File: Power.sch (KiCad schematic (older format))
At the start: 0 parts

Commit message: Blocked out the LED Driver and Power sheets
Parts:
- added C? (x2): C, ~, symbol C
- added F? (x4): FUSE, ~, symbol FUSE
- added L? (x2): INDUCTOR, ~, symbol INDUCTOR
- added P?: CONN_12X2, symbol CONN_12X2
- added R?: R, ~, symbol R
- added SW?: SWITCH_INV, ~, symbol SWITCH_INV
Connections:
- net labels added: +12P, +12V, +3.3V, +5V, -12P, -12V, GND
- wire segments 0 -> 43
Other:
- note added: "12V Power Filtering"
- note added: "24Pin Molex from ATX Power Supply"
- note added: "Main Power Switch"
- note added: "Power from ATX Power Supply\nFuses are PTC Resettable"

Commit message: Completed Arduino Block Diagram and Fan Redesign
The commits as of this are now up to date with the videos released for
Contextual Electronics, Week 3.
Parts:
- removed F? (x4): FUSE, ~, symbol FUSE
- added TH? (x4): THERMISTOR, ~, symbol THERMISTOR
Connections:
- net labels added: +12C
- wire segments 43 -> 44
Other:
- note added: "+12v for current sense\nin fan module"
- note added: "PTC Resettable\nFuses"
- note added: "Unfiltered Power Rails"
- note removed: "Power from ATX Power Supply\nFuses are PTC Resettable"
- moved on the sheet: C?, L?

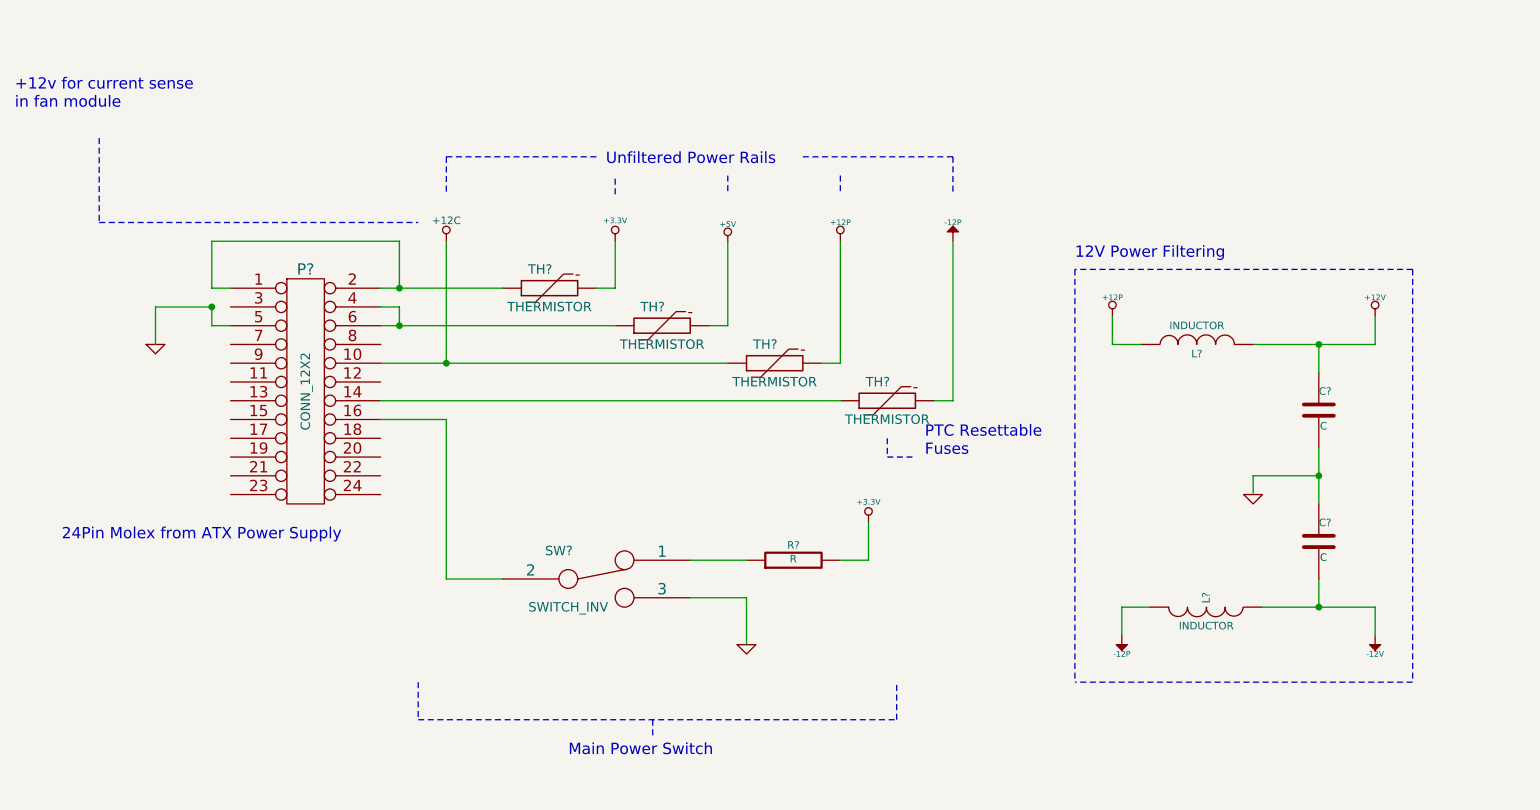
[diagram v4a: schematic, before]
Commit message: Initial layout of relay and thermocouple
All block diagrams completed through Week 3.  Component selection
spreadsheets created: Bench Buddy Session 1CE.xlsx = official part
selection and bom.xlsx is the version I came up with.

Part association and initial layout of the Relay and Thermocouple
sections completed.
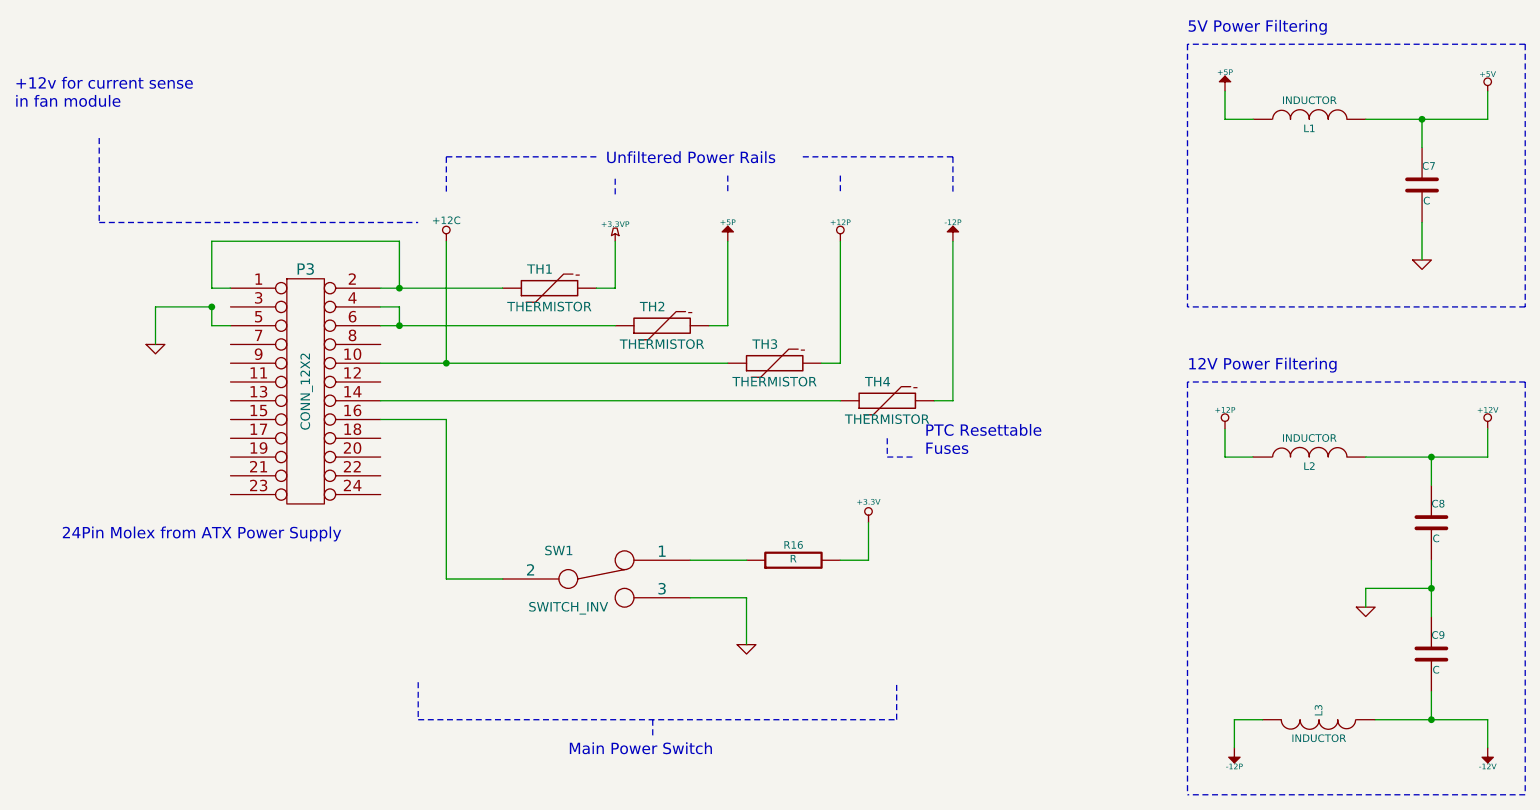
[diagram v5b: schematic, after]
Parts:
- removed C? (x2): C, ~, symbol C
- added C7, C8, C9: C, ~, symbol C
- added L1: INDUCTOR, ~, symbol INDUCTOR
- gave numbers to parts that had none: 9
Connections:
- net +12V: now also C8.1
- net +3.3V: no longer TH1.2
- net +5V: now also C7.1, L1.2; no longer TH2.2
- net -12V: now also C9.2
- net GND: now also C7.2, C8.2, C9.1
- new net +3.3VP: TH1.2
- new net +5P: L1.1, TH2.2
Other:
- note added: "5V Power Filtering"
- moved on the sheet: L2, L3

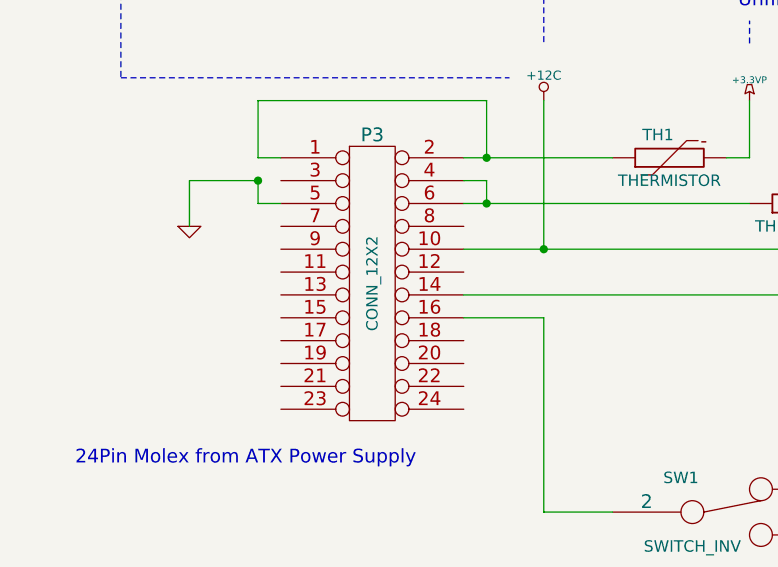
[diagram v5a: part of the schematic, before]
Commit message: Initial layout of Arduino and Fan-Current
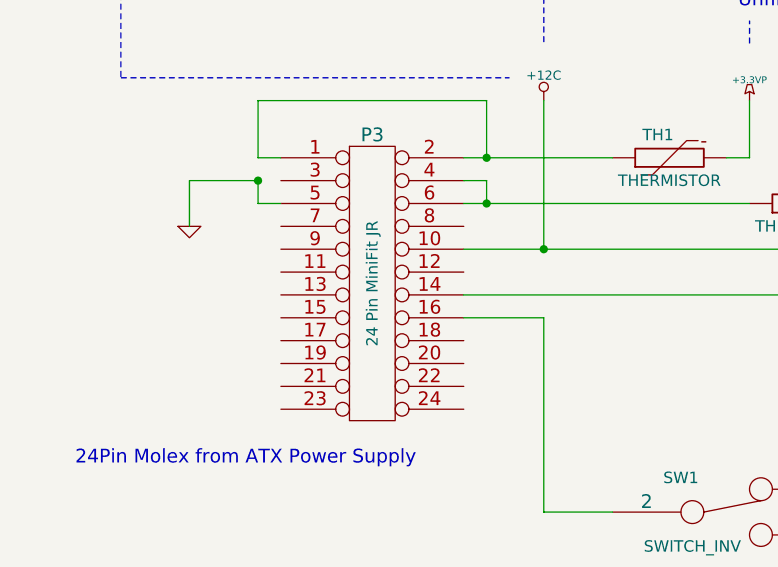
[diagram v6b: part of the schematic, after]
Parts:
- P3: value CONN_12X2 -> 24 Pin MiniFit JR; Distrib Part Num 1 (none) -> 538-39-30-1240; MFG Name (none) -> Molex; MFG Part Num (none) -> 39-30-1240
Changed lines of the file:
@@
 Sheet 4 9
 Title ""
-Date "21 feb 2014"
+Date "22 feb 2014"
 Rev ""
 Comp ""
@@
 P 3500 3750
 F 0 "P3" H 3500 4400 60  0000 C CNN
-F 1 "CONN_12X2" V 3500 3750 50  0000 C CNN
+F 1 "24 Pin MiniFit JR" V 3500 3750 50  0000 C CNN
 F 2 "" H 3500 3750 60  0000 C CNN
 F 3 "" H 3500 3750 60  0000 C CNN
+F 4 "Molex" H 3500 3750 60  0001 C CNN "MFG Name"
+F 5 "39-30-1240" H 3500 3750 60  0001 C CNN "MFG Part Num"
+F 6 "538-39-30-1240" H 3500 3750 60  0001 C CNN "Distrib Part Num 1"
 	1    3500 3750
 	1    0    0    -1

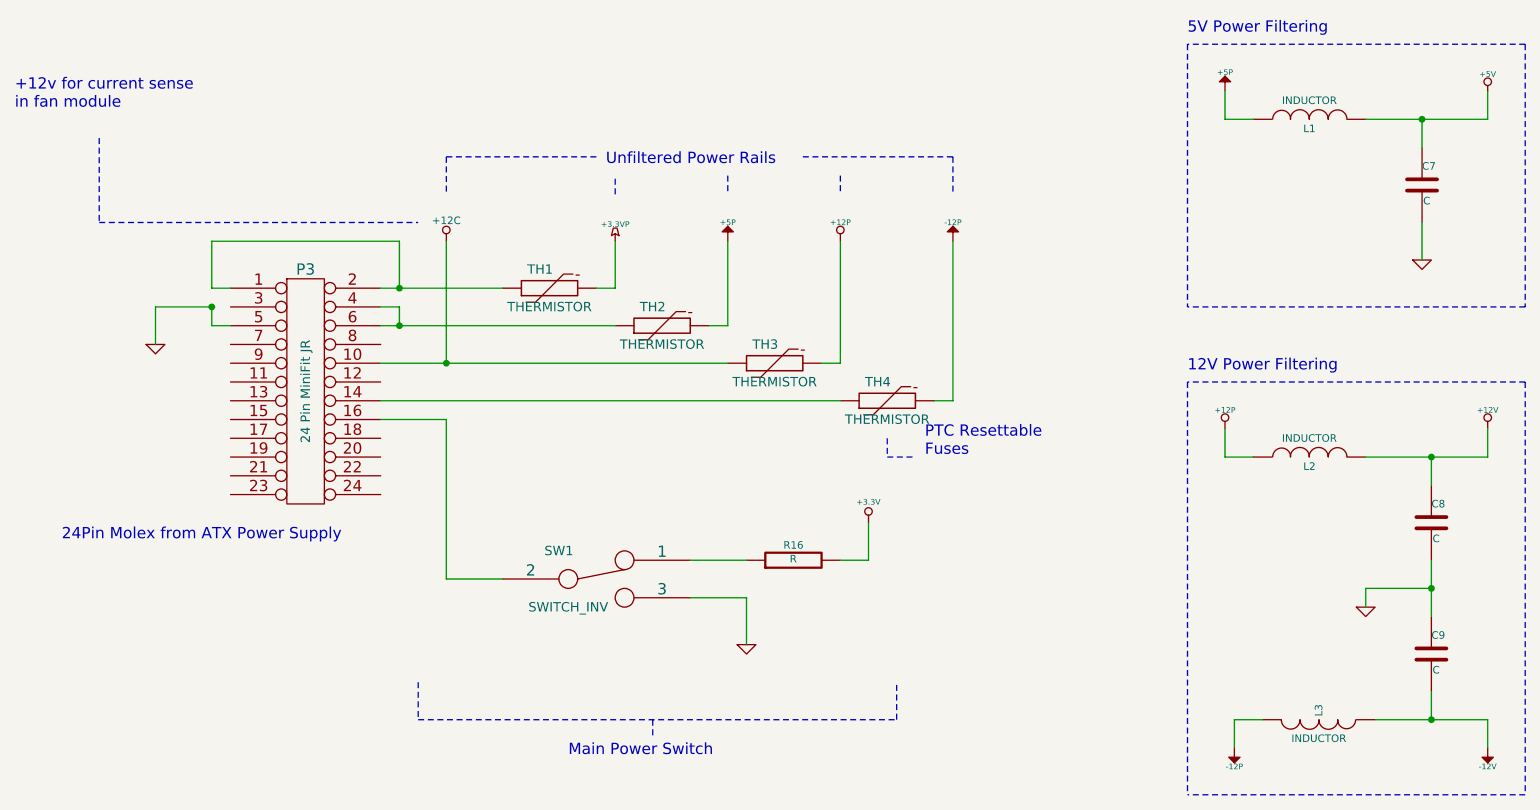
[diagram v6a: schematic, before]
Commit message: Reorganization of power conditioning module
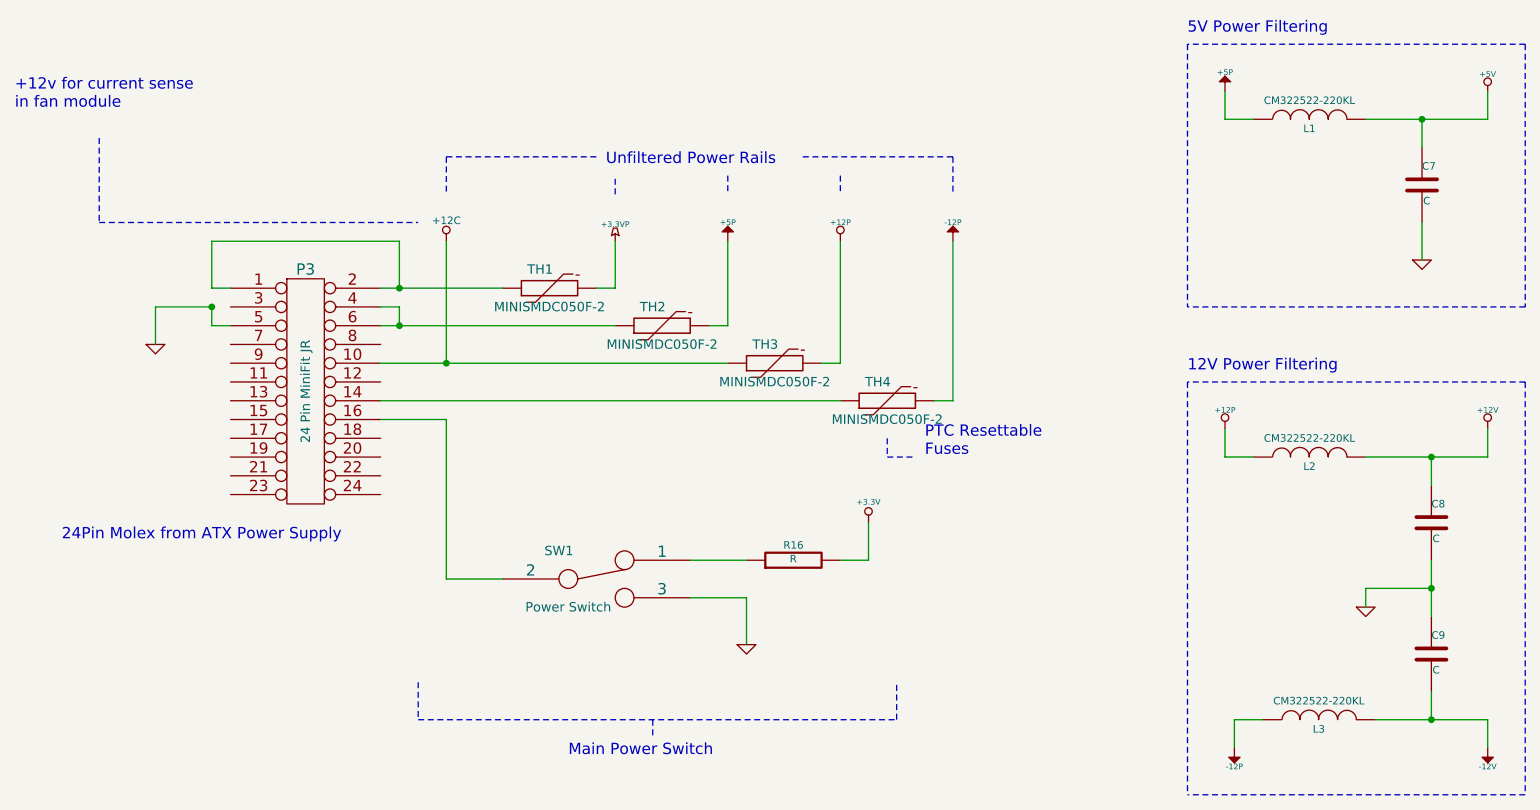
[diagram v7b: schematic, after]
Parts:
- L1, L2, L3: value INDUCTOR -> CM322522-220KL; Distrib Part Num 1 (none) -> CM322522-220KLCT; Distrib Part Num 1 Link (none) -> http://www.bourns.com/data/global/pdfs/cm.pdf; MFG Name (none) -> Bournes Inc.; MFG Part Num (none) -> CM322522-220KL
- SW1: value SWITCH_INV -> Power Switch; Distrib Part Num 1 (none) -> CKN9559; Distrib Part Num 1 Link (none) -> http://www.ck-components.com/index.php?module=media&action=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; MFG Name (none) -> C&K Components; MFG Part Num (none) -> OS102011MA1QN1
- TH1, TH2, TH3, TH4: value THERMISTOR -> MINISMDC050F-2; Distrib Part Num 1 (none) -> MINISMDC050FCT; Distrib Part Num 1 Link (none) -> http://documents.tycoelectronics.com/commerce/DocumentDeliv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; MFG Name (none) -> TE Connectivity; MFG Part Num (none) -> MINISMDC050F-2
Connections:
- net -12P: now also L3.1; no longer L3.2
- net -12V: now also L3.2; no longer L3.1
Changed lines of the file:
@@
 P 5050 4750
 F 0 "SW1" H 4850 4900 50  0000 C CNN
-F 1 "SWITCH_INV" H 4900 4600 50  0000 C CNN
+F 1 "Power Switch" H 4900 4600 50  0000 C CNN
 F 2 "~" H 5050 4750 60  0000 C CNN
 F 3 "~" H 5050 4750 60  0000 C CNN
+F 4 "C&K Components" H 5050 4750 60  0001 C CNN "MFG Name"
+F 5 "OS102011MA1QN1" H 5050 4750 60  0001 C CNN "MFG Part Num"
+F 6 "CKN9559" H 5050 4750 60  0001 C CNN "Distrib Part Num 1"
+F 7 "http://www.ck-components.com/index.php?module=media&action=Display&cmpref=14388&lang=en&width=&height=&format=&alt=" H 5050 4750 60  0001 C CNN "Distrib Part Num 1 Link"
 	1    5050 4750
 	1    0    0    -1
@@
 	1    0    0    -1
 $EndComp
-$Comp
-L INDUCTOR L2
-U 1 1 52F2FF42
-P 8850 4100
-F 0 "L2" V 8800 4100 40  0000 C CNN
-F 1 "INDUCTOR" V 8950 4100 40  0000 C CNN
-F 2 "~" H 8850 4100 60  0000 C CNN
-F 3 "~" H 8850 4100 60  0000 C CNN
-	1    8850 4100
-	0    -1   -1   0
-$EndComp
-$Comp
-L INDUCTOR L3
-U 1 1 52F2FF48
-P 8900 5500
-F 0 "L3" H 8850 5500 40  0000 C CNN
-F 1 "INDUCTOR" V 9000 5500 40  0000 C CNN
-F 2 "~" H 8900 5500 60  0000 C CNN
-F 3 "~" H 8900 5500 60  0000 C CNN
-	1    8900 5500
-	0    1    1    0
-$EndComp
 Wire Wire Line
 	8400 3950 8400 4100
@@
 P 4800 3200
 F 0 "TH1" V 4900 3250 50  0000 C CNN
-F 1 "THERMISTOR" V 4700 3200 50  0000 C CNN
+F 1 "MINISMDC050F-2" V 4700 3200 50  0000 C CNN
 F 2 "~" H 4800 3200 60  0000 C CNN
 F 3 "~" H 4800 3200 60  0000 C CNN
+F 4 "TE Connectivity" H 4800 3200 60  0001 C CNN "MFG Name"
+F 5 "MINISMDC050F-2" H 4800 3200 60  0001 C CNN "MFG Part Num"
+F 6 "MINISMDC050FCT" H 4800 3200 60  0001 C CNN "Distrib Part Num 1"
+F 7 "http://documents.tycoelectronics.com/commerce/DocumentDelivery/DDEController?Action=showdoc&DocId=Specification+Or+Standard%7FSCD25063%7FH%7Fpdf%7FEnglish%7FENG_SS_SCD25063_H.pdf" H 4800 3200 60  0001 C CNN "Distrib Part Num 1 Link"
 	1    4800 3200
-	0    -1   -1   0
-$EndComp
-$Comp
-L THERMISTOR TH2
-U 1 1 52F410C0
-P 5400 3400
-F 0 "TH2" V 5500 3450 50  0000 C CNN
-F 1 "THERMISTOR" V 5300 3400 50  0000 C CNN
-F 2 "~" H 5400 3400 60  0000 C CNN
-F 3 "~" H 5400 3400 60  0000 C CNN
-	1    5400 3400
-	0    -1   -1   0
-$EndComp
-$Comp
-L THERMISTOR TH3
-U 1 1 52F410C6
-P 6000 3600
-F 0 "TH3" V 6100 3650 50  0000 C CNN
-F 1 "THERMISTOR" V 5900 3600 50  0000 C CNN
-F 2 "~" H 6000 3600 60  0000 C CNN
-F 3 "~" H 6000 3600 60  0000 C CNN
-	1    6000 3600
-	0    -1   -1   0
-$EndComp
-$Comp
-L THERMISTOR TH4
-U 1 1 52F410CC
-P 6600 3800
-F 0 "TH4" V 6700 3850 50  0000 C CNN
-F 1 "THERMISTOR" V 6500 3800 50  0000 C CNN
-F 2 "~" H 6600 3800 60  0000 C CNN
-F 3 "~" H 6600 3800 60  0000 C CNN
-	1    6600 3800
 	0    -1   -1   0
 $EndComp
@@
 P 8850 2300
 F 0 "L1" V 8800 2300 40  0000 C CNN
-F 1 "INDUCTOR" V 8950 2300 40  0000 C CNN
+F 1 "CM322522-220KL" V 8950 2300 40  0000 C CNN
 F 2 "~" H 8850 2300 60  0000 C CNN
 F 3 "~" H 8850 2300 60  0000 C CNN
+F 4 "Bournes Inc." H 8850 2300 60  0001 C CNN "MFG Name"
+F 5 "CM322522-220KL" H 8850 2300 60  0001 C CNN "MFG Part Num"
+F 6 "CM322522-220KLCT" H 8850 2300 60  0001 C CNN "Distrib Part Num 1"
+F 7 "http://www.bourns.com/data/global/pdfs/cm.pdf" H 8850 2300 60  0001 C CNN "Distrib Part Num 1 Link"
 	1    8850 2300
 	0    -1   -1   0
@@
 	1    0    0    -1
 $EndComp
+$Comp
+L THERMISTOR TH2
+U 1 1 53092775
+P 5400 3400
+F 0 "TH2" V 5500 3450 50  0000 C CNN
+F 1 "MINISMDC050F-2" V 5300 3400 50  0000 C CNN
+F 2 "~" H 5400 3400 60  0000 C CNN
+F 3 "~" H 5400 3400 60  0000 C CNN
+F 4 "TE Connectivity" H 5400 3400 60  0001 C CNN "MFG Name"
+F 5 "MINISMDC050F-2" H 5400 3400 60  0001 C CNN "MFG Part Num"
+F 6 "MINISMDC050FCT" H 5400 3400 60  0001 C CNN "Distrib Part Num 1"
+F 7 "http://documents.tycoelectronics.com/commerce/DocumentDelivery/DDEController?Action=showdoc&DocId=Specification+Or+Standard%7FSCD25063%7FH%7Fpdf%7FEnglish%7FENG_SS_SCD25063_H.pdf" H 5400 3400 60  0001 C CNN "Distrib Part Num 1 Link"
+	1    5400 3400
+	0    -1   -1   0
+$EndComp
+$Comp
+L THERMISTOR TH3
+U 1 1 5309277F
+P 6000 3600
+F 0 "TH3" V 6100 3650 50  0000 C CNN
+F 1 "MINISMDC050F-2" V 5900 3600 50  0000 C CNN
+F 2 "~" H 6000 3600 60  0000 C CNN
+F 3 "~" H 6000 3600 60  0000 C CNN
+F 4 "TE Connectivity" H 6000 3600 60  0001 C CNN "MFG Name"
+F 5 "MINISMDC050F-2" H 6000 3600 60  0001 C CNN "MFG Part Num"
+F 6 "MINISMDC050FCT" H 6000 3600 60  0001 C CNN "Distrib Part Num 1"
+F 7 "http://documents.tycoelectronics.com/commerce/DocumentDelivery/DDEController?Action=showdoc&DocId=Specification+Or+Standard%7FSCD25063%7FH%7Fpdf%7FEnglish%7FENG_SS_SCD25063_H.pdf" H 6000 3600 60  0001 C CNN "Distrib Part Num 1 Link"
+	1    6000 3600
+	0    -1   -1   0
+$EndComp
+$Comp
+L THERMISTOR TH4
+U 1 1 53092789
+P 6600 3800
+F 0 "TH4" V 6700 3850 50  0000 C CNN
+F 1 "MINISMDC050F-2" V 6500 3800 50  0000 C CNN
+F 2 "~" H 6600 3800 60  0000 C CNN
+F 3 "~" H 6600 3800 60  0000 C CNN
+F 4 "TE Connectivity" H 6600 3800 60  0001 C CNN "MFG Name"
+F 5 "MINISMDC050F-2" H 6600 3800 60  0001 C CNN "MFG Part Num"
+F 6 "MINISMDC050FCT" H 6600 3800 60  0001 C CNN "Distrib Part Num 1"
+F 7 "http://documents.tycoelectronics.com/commerce/DocumentDelivery/DDEController?Action=showdoc&DocId=Specification+Or+Standard%7FSCD25063%7FH%7Fpdf%7FEnglish%7FENG_SS_SCD25063_H.pdf" H 6600 3800 60  0001 C CNN "Distrib Part Num 1 Link"
+	1    6600 3800
+	0    -1   -1   0
+$EndComp
+$Comp
+L INDUCTOR L2
+U 1 1 53092812
+P 8850 4100
+F 0 "L2" V 8800 4100 40  0000 C CNN
+F 1 "CM322522-220KL" V 8950 4100 40  0000 C CNN
+F 2 "~" H 8850 4100 60  0000 C CNN
+F 3 "~" H 8850 4100 60  0000 C CNN
+F 4 "Bournes Inc." H 8850 4100 60  0001 C CNN "MFG Name"
+F 5 "CM322522-220KL" H 8850 4100 60  0001 C CNN "MFG Part Num"
+F 6 "CM322522-220KLCT" H 8850 4100 60  0001 C CNN "Distrib Part Num 1"
+F 7 "http://www.bourns.com/data/global/pdfs/cm.pdf" H 8850 4100 60  0001 C CNN "Distrib Part Num 1 Link"
+	1    8850 4100
+	0    -1   -1   0
+$EndComp
+$Comp
+L INDUCTOR L3
+U 1 1 5309281C
+P 8900 5500
+F 0 "L3" V 8850 5500 40  0000 C CNN
+F 1 "CM322522-220KL" V 9000 5500 40  0000 C CNN
+F 2 "~" H 8900 5500 60  0000 C CNN
+F 3 "~" H 8900 5500 60  0000 C CNN
+F 4 "Bournes Inc." H 8900 5500 60  0001 C CNN "MFG Name"
+F 5 "CM322522-220KL" H 8900 5500 60  0001 C CNN "MFG Part Num"
+F 6 "CM322522-220KLCT" H 8900 5500 60  0001 C CNN "Distrib Part Num 1"
+F 7 "http://www.bourns.com/data/global/pdfs/cm.pdf" H 8900 5500 60  0001 C CNN "Distrib Part Num 1 Link"
+	1    8900 5500
+	0    -1   -1   0
+$EndComp
 $EndSCHEMATC
